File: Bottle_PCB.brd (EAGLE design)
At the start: 100 x 50 mm, 75 parts, among them J1 GROVE-4P-2.0-SMD, Q1 8.000 MHz, Q2 ZVN 3306 F, Q3 ZVN 3306 F, Q4 ZVN 3306 F, Q5 ZVN 3306 F, Q6 ZVN 3306 F, Q7 ZVN 3306 F, U1 USD-SOCKETNEW

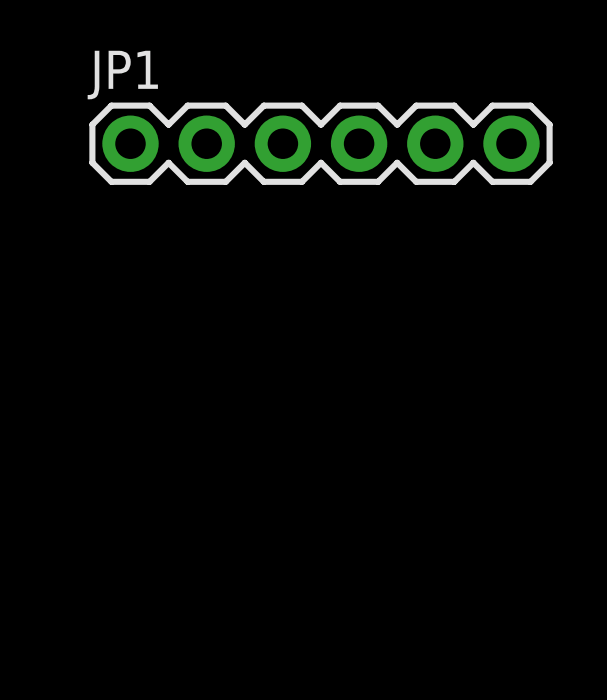
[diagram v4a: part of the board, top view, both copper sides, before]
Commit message: - connected FTDI and XBEE Socket
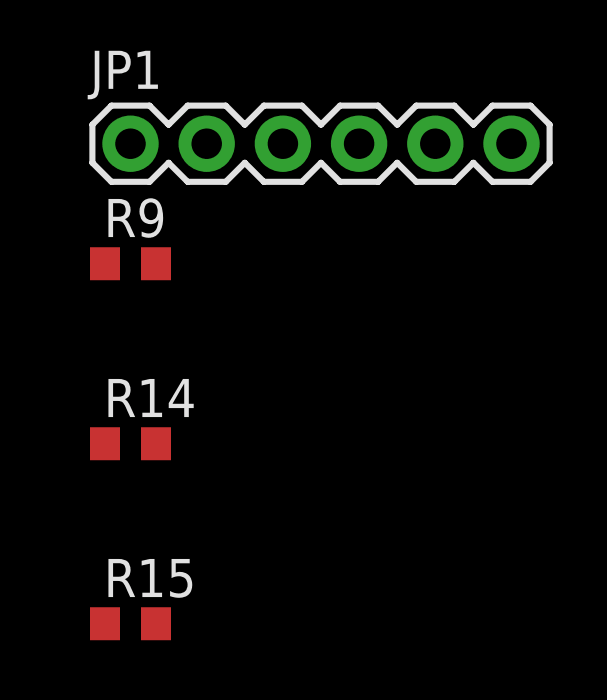
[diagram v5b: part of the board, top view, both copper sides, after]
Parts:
- added R14, R15, R9: 1k, resistor:R0603
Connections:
- removed net BEE_PAIR: XBEE_SOCKET.9
- new net BEE_DTR: R9.2, XBEE_SOCKET.9
- new net FTDI_RTS: R15.2, UART1_IC2.3
- new net N$5: R14.1, XBEE_SOCKET.12
- new net N$7: R15.1, XBEE_SOCKET.16
- net FTDI_CTS: now also R14.2
- net FTDI_DTR: now also R9.1
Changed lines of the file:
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@@
 <element name="C11" library="quantum-sensor" package="C0805" value="100n" x="-31" y="-92"/>
 <element name="JP1" library="SparkFun-Connectors" package="1X06" value="" x="-31" y="-99"/>
+<element name="R9" library="resistor" package="R0603" value="1k" x="-31" y="-103">
+<attribute name="SPICEPREFIX" value="R" x="-31" y="-103" size="1.778" layer="27" display="off"/>
+</element>
+<element name="R14" library="resistor" package="R0603" value="1k" x="-31" y="-109">
+<attribute name="SPICEPREFIX" value="R" x="-31" y="-109" size="1.778" layer="27" display="off"/>
+</element>
+<element name="R15" library="resistor" package="R0603" value="1k" x="-31" y="-115">
+<attribute name="SPICEPREFIX" value="R" x="-31" y="-115" size="1.778" layer="27" display="off"/>
+</element>
 </elements>
 <signals>
@@
 <wire x1="67.818" y1="29.4495" x2="67.5495" y2="29.718" width="0.4064" layer="1"/>
 <contactref element="JP1" pad="DTR"/>
+<contactref element="R9" pad="1"/>
+<wire x1="-31" y1="-99" x2="-31.85" y2="-103" width="0" layer="19" extent="1-1"/>
 <wire x1="67.818" y1="29.4495" x2="-31" y2="-99" width="0" layer="19" extent="1-1"/>
 </signal>
@@
 <contactref element="XBEE_SOCKET" pad="20"/>
 </signal>
-<signal name="BEE_PAIR">
+<signal name="BEE_DTR">
 <contactref element="XBEE_SOCKET" pad="9"/>
+<contactref element="R9" pad="2"/>
+<wire x1="-32.5" y1="-59" x2="-30.15" y2="-103" width="0" layer="19" extent="1-1"/>
 </signal>
 <signal name="FTDI_CTS">
 <contactref element="UART1_IC2" pad="11"/>
 <contactref element="JP1" pad="CTS"/>
+<contactref element="R14" pad="2"/>
+<wire x1="-20.84" y1="-99" x2="-30.15" y2="-109" width="0" layer="19" extent="1-1"/>
 <wire x1="71.432" y1="23.633" x2="-20.84" y2="-99" width="0" layer="19" extent="1-1"/>
 </signal>
+<signal name="N$5">
+<contactref element="XBEE_SOCKET" pad="12"/>
+<contactref element="R14" pad="1"/>
+<wire x1="-10.5" y1="-59" x2="-31.85" y2="-109" width="0" layer="19" extent="1-1"/>
+</signal>
+<signal name="FTDI_RTS">
+<contactref element="UART1_IC2" pad="3"/>
+<contactref element="R15" pad="2"/>
+<wire x1="71.432" y1="28.833" x2="-30.15" y2="-115" width="0" layer="19" extent="1-1"/>
+</signal>
+<signal name="N$7">
+<contactref element="XBEE_SOCKET" pad="16"/>
+<contactref element="R15" pad="1"/>
+<wire x1="-10.5" y1="-51" x2="-31.85" y2="-115" width="0" layer="19" extent="1-1"/>
+</signal>
 </signals>

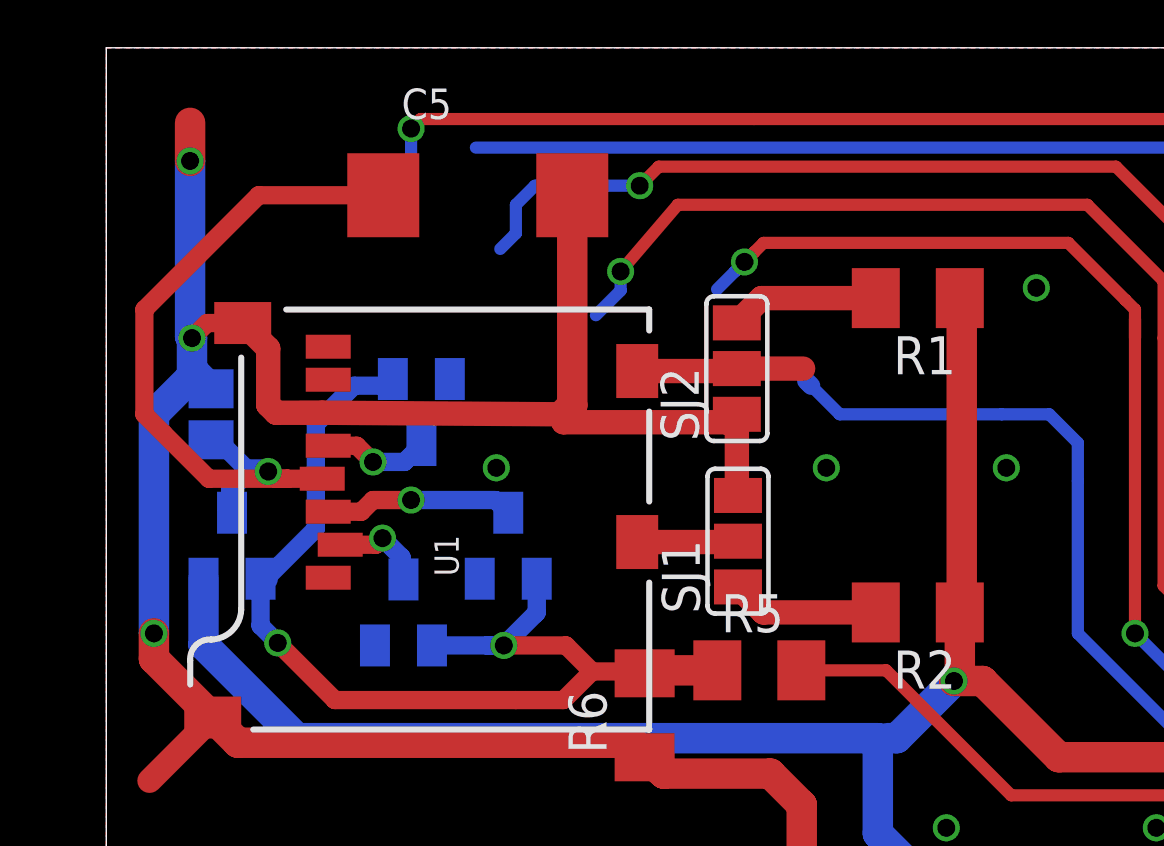
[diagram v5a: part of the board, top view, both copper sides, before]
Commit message: - overhauled and simplified SD card connection - decided to stick with the sparkfun socket, as it's cheap and available by now
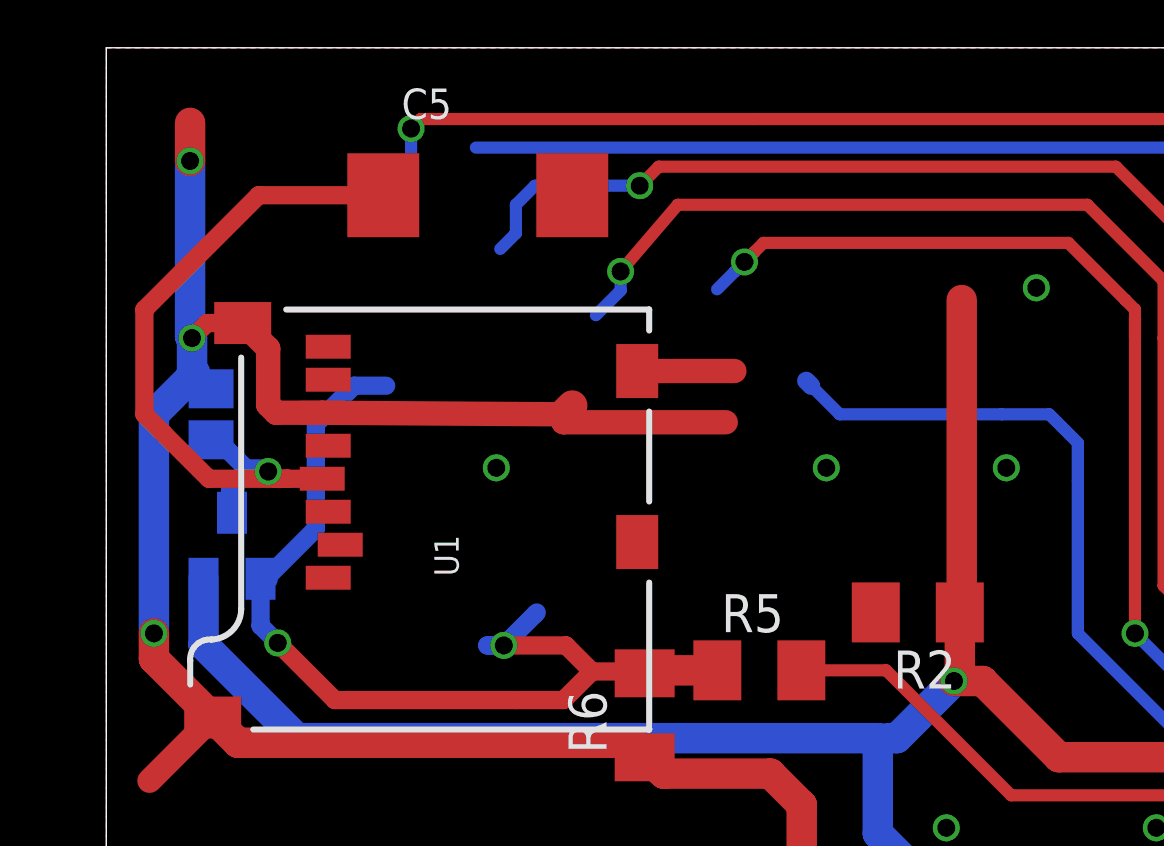
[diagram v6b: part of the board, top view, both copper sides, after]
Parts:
- removed Q2, Q3, Q4: ZVN 3306 F, transistor-small-signal:SOT23
- removed R1: 50k, rcl:M1206
- removed SJ1, SJ2: (no value), jumper:SJ_2
- R2: value 50k -> 10k
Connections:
- net SD_OFF renamed PC2_SD_OFF
- removed net N$16: SJ2.2, U1.CD1
- removed net N$17: SJ1.2, U1.CD2
- removed net N$21: R1.2, SJ2.3
- removed net N$22: R2.2, SJ1.1
- removed net N$28: Q4.3, U1.2
- removed net N$29: Q3.3, U1.3
- removed net N$30: Q2.3, U1.5
- new net PC3_SD_CD: ATMEGA1284.22, R2.2, U1.CD1, U1.CD2
- net +3V3: no longer R1.1
- net GND: no longer SJ1.3, SJ2.1
- net N$33: no longer Q2.1, Q3.1, Q4.1
- net PD3_TXD1/MOSI: now also U1.3; no longer Q3.2
- net PD4_XCK1/SCK: now also U1.5; no longer Q2.2
- net PD5_CS: now also U1.2; no longer Q4.2
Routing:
- net GND: track 428.0 -> 417.1 mm
- net N$29: track 6.34 -> 0.00 mm, vias 1 -> 0
- net N$16: track 5.56 -> 0.00 mm
- net N$21: track 4.97 -> 0.00 mm
- net N$22: track 4.95 -> 0.00 mm
- net N$30: track 3.56 -> 0.00 mm, vias 1 -> 0
- net N$17: track 3.37 -> 0.00 mm
- net N$33: track 36.7 -> 33.5 mm
- net PC3_SD_CD: track 0.00 -> 3.24 mm
- net N$28: track 3.17 -> 0.00 mm, vias 1 -> 0

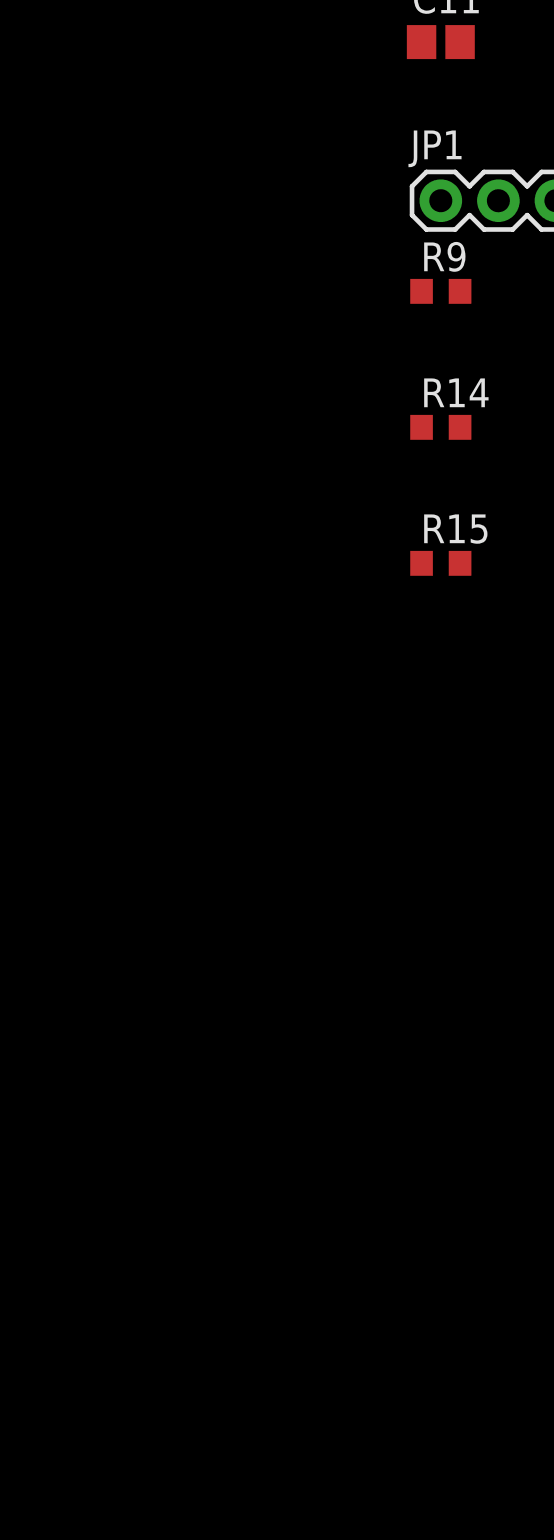
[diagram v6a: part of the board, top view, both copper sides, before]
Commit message: - added HM11 BT Module - employed component device exported from SeedStudio BLE_Bee_v1.0 schematic
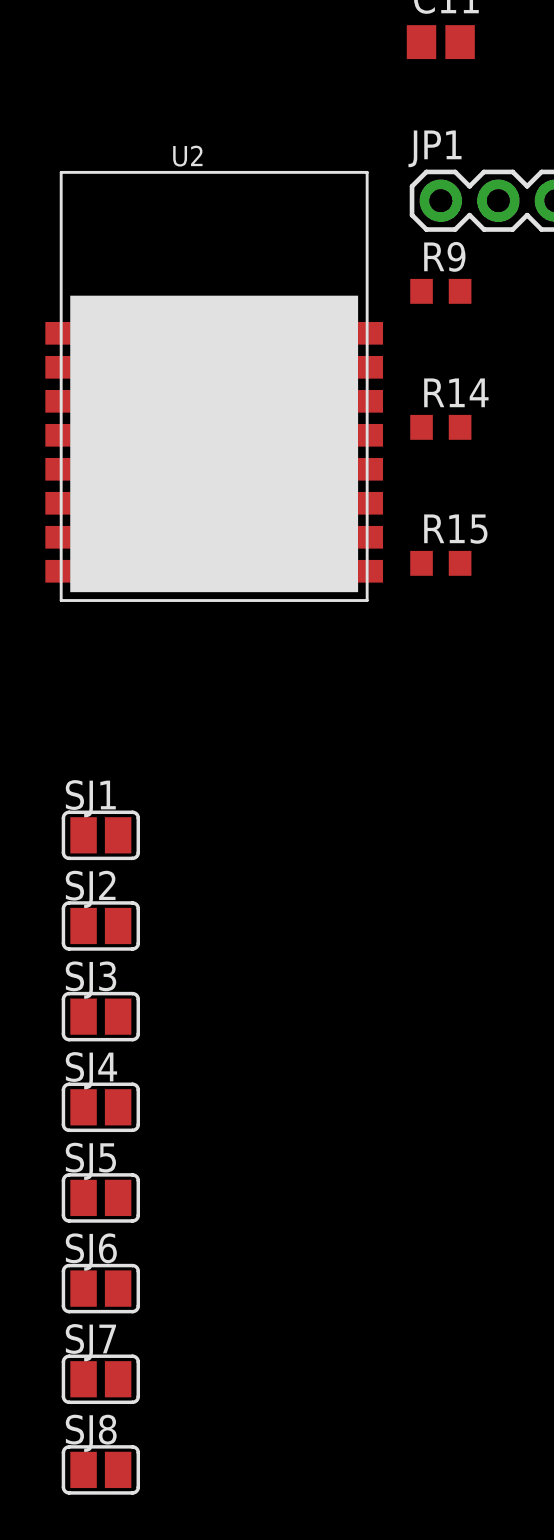
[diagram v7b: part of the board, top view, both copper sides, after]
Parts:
- added SJ1, SJ2, SJ3, SJ4, SJ5, SJ6, SJ7, SJ8: (no value), jumper:SJ
- added U2: (no value), Seed-HM11:16P-18.5X13.5X0.8
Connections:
- new net N$16: SJ1.2, U2.1
- new net N$17: SJ2.2, U2.2
- new net N$19: SJ3.2, U2.3
- new net N$20: SJ4.2, U2.4
- new net N$21: SJ5.2, U2.9
- new net N$24: SJ8.2, U2.11
- new net N$25: SJ6.2, U2.15
- new net N$26: SJ7.2, U2.16
- net BEE_RESET: now also SJ8.1
- net BEE_STATUS: now also SJ6.1
- net BEE_VCC: now also SJ5.1
- net FTDI_CTS: now also SJ3.1
- net FTDI_DTR: now also SJ7.1
- net FTDI_RTS: now also SJ1.1
- net GND: now also U2.12
- net PD0_RXD0_USB: now also SJ2.1
- net PD1_TXD0_USB: now also SJ4.1
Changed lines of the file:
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@@
 <layer number="56" name="wert" color="7" fill="1" visible="no" active="yes"/>
 <layer number="57" name="tCAD" color="7" fill="1" visible="no" active="no"/>
+<layer number="90" name="Modules" color="5" fill="1" visible="no" active="no"/>
 <layer number="91" name="Nets" color="2" fill="1" visible="no" active="no"/>
 <layer number="92" name="Busses" color="1" fill="1" visible="no" active="no"/>
@@
 <attribute name="SPICEPREFIX" value="R" x="-31" y="-115" size="1.778" layer="27" display="off"/>
 </element>
+<element name="U2" library="Seed-HM11" package="16P-18.5X13.5X0.8" value="" x="-41" y="-107"/>
+<element name="SJ1" library="jumper" package="SJ" value="" x="-46" y="-127"/>
+<element name="SJ2" library="jumper" package="SJ" value="" x="-46" y="-131"/>
+<element name="SJ3" library="jumper" package="SJ" value="" x="-46" y="-135"/>
+<element name="SJ4" library="jumper" package="SJ" value="" x="-46" y="-139"/>
+<element name="SJ5" library="jumper" package="SJ" value="" x="-46" y="-143"/>
+<element name="SJ6" library="jumper" package="SJ" value="" x="-46" y="-147"/>
+<element name="SJ7" library="jumper" package="SJ" value="" x="-46" y="-151"/>
+<element name="SJ8" library="jumper" package="SJ" value="" x="-46" y="-155"/>
 </elements>
 <signals>
@@
 <contactref element="C4" pad="2"/>
 <contactref element="C5" pad="-"/>
+<contactref element="U2" pad="12"/>
+<wire x1="-31.85" y1="-92" x2="-34.4" y2="-110.85" width="0" layer="19" extent="1-1"/>
 <wire x1="-31.2512" y1="-87.2606" x2="-31.85" y2="-92" width="0" layer="19" extent="1-1"/>
 <wire x1="-24.7488" y1="-87.2606" x2="-31.2512" y2="-87.2606" width="0" layer="19" extent="1-1"/>
@@
 <contactref element="JP1" pad="DTR"/>
 <contactref element="R9" pad="1"/>
+<contactref element="SJ7" pad="1"/>
+<wire x1="-31.85" y1="-103" x2="-46.762" y2="-151" width="0" layer="19" extent="1-1"/>
 <wire x1="-31" y1="-99" x2="-31.85" y2="-103" width="0" layer="19" extent="1-1"/>
 <wire x1="67.818" y1="29.4495" x2="-31" y2="-99" width="0" layer="19" extent="1-1"/>
@@
 <contactref element="R13" pad="1"/>
 <contactref element="JP1" pad="RXI"/>
+<contactref element="SJ4" pad="1"/>
+<wire x1="-28.46" y1="-99" x2="-46.762" y2="-139" width="0" layer="19" extent="1-1"/>
 <wire x1="-31.85" y1="-77" x2="-28.46" y2="-99" width="0" layer="19" extent="1-1"/>
 <wire x1="-1.35" y1="-11" x2="-31.85" y2="-77" width="0" layer="19" extent="1-1"/>
@@
 <contactref element="R12" pad="1"/>
 <contactref element="JP1" pad="TXO"/>
+<contactref element="SJ2" pad="1"/>
+<wire x1="-25.92" y1="-99" x2="-46.762" y2="-131" width="0" layer="19" extent="1-1"/>
 <wire x1="-31.85" y1="-73" x2="-25.92" y2="-99" width="0" layer="19" extent="1-1"/>
 <wire x1="51.8375" y1="23.6725" x2="-31.85" y2="-73" width="0" layer="19" extent="1-1"/>
@@
 <contactref element="SW_BEE_RST" pad="1"/>
 <contactref element="R7" pad="1"/>
+<contactref element="SJ8" pad="1"/>
+<wire x1="-30.15" y1="-92" x2="-46.762" y2="-155" width="0" layer="19" extent="1-1"/>
 <wire x1="-31.2512" y1="-82.7394" x2="-30.15" y2="-92" width="0" layer="19" extent="1-1"/>
 <wire x1="-24.7488" y1="-82.7394" x2="-31.2512" y2="-82.7394" width="0" layer="19" extent="1-1"/>
@@
 <contactref element="C8" pad="1"/>
 <contactref element="C10" pad="+"/>
+<contactref element="SJ5" pad="1"/>
+<wire x1="-32.5" y1="-43" x2="-46.762" y2="-143" width="0" layer="19" extent="1-1"/>
 <wire x1="21.375" y1="5.715" x2="-32.5" y2="-43" width="0" layer="19" extent="1-1"/>
 <wire x1="24.3975" y1="6.25" x2="21.375" y2="5.715" width="0" layer="19" extent="1-16"/>
@@
 <signal name="BEE_STATUS">
 <contactref element="XBEE_SOCKET" pad="19"/>
+<contactref element="SJ6" pad="1"/>
+<wire x1="-7.5" y1="-45" x2="-46.762" y2="-147" width="0" layer="19" extent="1-1"/>
 </signal>
 <signal name="BEE_MODE">
@@
 <contactref element="JP1" pad="CTS"/>
 <contactref element="R14" pad="2"/>
+<contactref element="SJ3" pad="1"/>
+<wire x1="-30.15" y1="-109" x2="-46.762" y2="-135" width="0" layer="19" extent="1-1"/>
 <wire x1="-20.84" y1="-99" x2="-30.15" y2="-109" width="0" layer="19" extent="1-1"/>
 <wire x1="71.432" y1="23.633" x2="-20.84" y2="-99" width="0" layer="19" extent="1-1"/>
@@
 <contactref element="UART1_IC2" pad="3"/>
 <contactref element="R15" pad="2"/>
+<contactref element="SJ1" pad="1"/>
+<wire x1="-30.15" y1="-115" x2="-46.762" y2="-127" width="0" layer="19" extent="1-1"/>
 <wire x1="71.432" y1="28.833" x2="-30.15" y2="-115" width="0" layer="19" extent="1-1"/>
 </signal>
@@
 <wire x1="-10.5" y1="-51" x2="-31.85" y2="-115" width="0" layer="19" extent="1-1"/>
 </signal>
+<signal name="N$16">
+<contactref element="SJ1" pad="2"/>
+<contactref element="U2" pad="1"/>
+<wire x1="-47.6" y1="-104.85" x2="-45.238" y2="-127" width="0" layer="19" extent="1-1"/>
+</signal>
+<signal name="N$17">
+<contactref element="SJ2" pad="2"/>
+<contactref element="U2" pad="2"/>
+<wire x1="-47.6" y1="-106.35" x2="-45.238" y2="-131" width="0" layer="19" extent="1-1"/>
+</signal>
+<signal name="N$19">
+<contactref element="SJ3" pad="2"/>
+<contactref element="U2" pad="3"/>
+<wire x1="-47.6" y1="-107.85" x2="-45.238" y2="-135" width="0" layer="19" extent="1-1"/>
+</signal>
+<signal name="N$20">
+<contactref element="SJ4" pad="2"/>
+<contactref element="U2" pad="4"/>
+<wire x1="-47.6" y1="-109.35" x2="-45.238" y2="-139" width="0" layer="19" extent="1-1"/>
+</signal>
+<signal name="N$21">
+<contactref element="U2" pad="9"/>
+<contactref element="SJ5" pad="2"/>
+<wire x1="-34.4" y1="-115.35" x2="-45.238" y2="-143" width="0" layer="19" extent="1-1"/>
+</signal>
+<signal name="N$24">
+<contactref element="SJ8" pad="2"/>
+<contactref element="U2" pad="11"/>
+<wire x1="-34.4" y1="-112.35" x2="-45.238" y2="-155" width="0" layer="19" extent="1-1"/>
+</signal>
+<signal name="N$25">
+<contactref element="U2" pad="15"/>
+<contactref element="SJ6" pad="2"/>
+<wire x1="-34.4" y1="-106.35" x2="-45.238" y2="-147" width="0" layer="19" extent="1-1"/>
+</signal>
+<signal name="N$26">
+<contactref element="U2" pad="16"/>
+<contactref element="SJ7" pad="2"/>
+<wire x1="-34.4" y1="-104.85" x2="-45.238" y2="-151" width="0" layer="19" extent="1-1"/>
+</signal>
 </signals>
